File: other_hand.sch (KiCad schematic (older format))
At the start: 49 parts

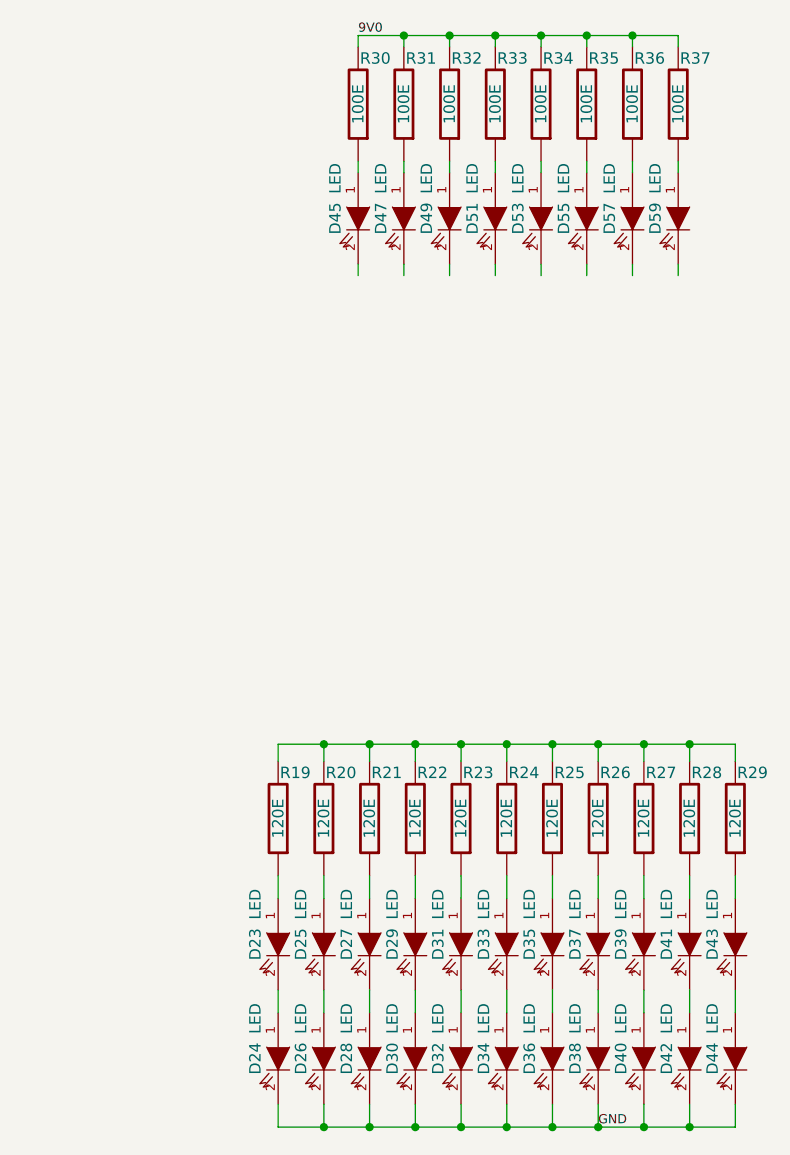
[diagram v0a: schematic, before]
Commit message: added the second Hand
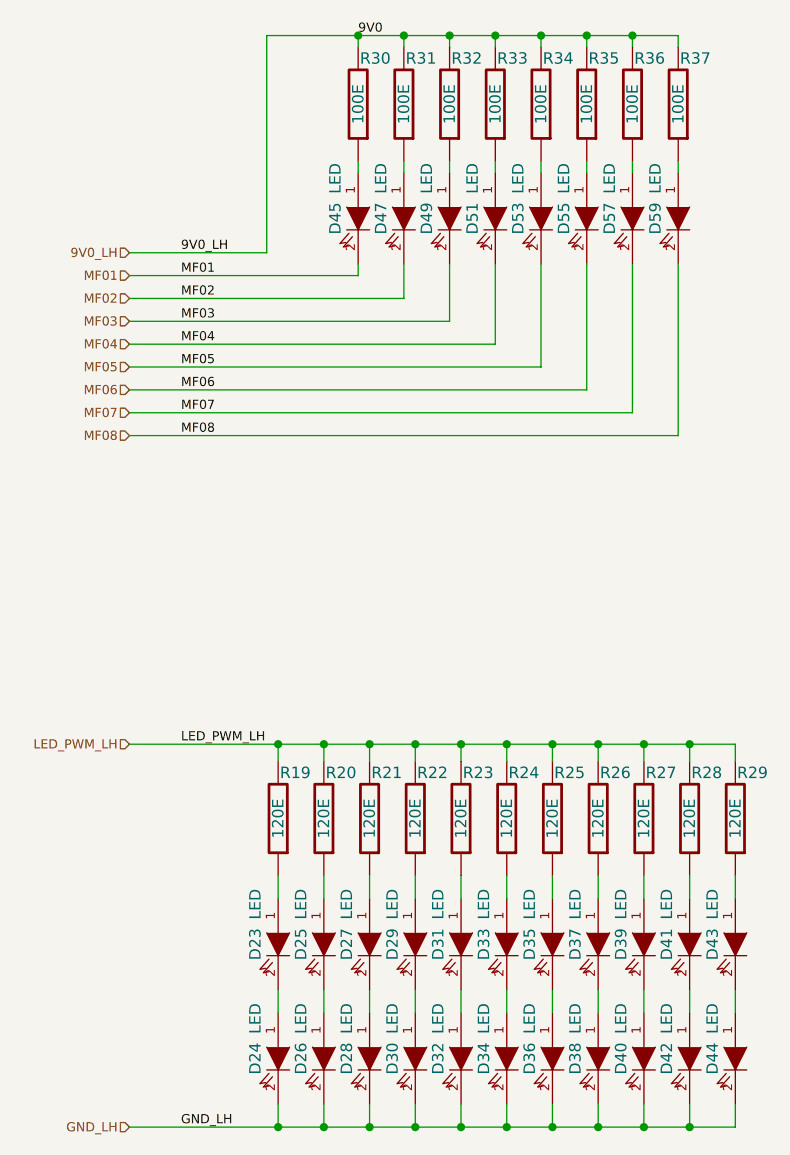
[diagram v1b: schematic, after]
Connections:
- net labels added: 9V0_LH, GND_LH, LED_PWM_LH, MF01, MF02, MF03, MF04, MF05, MF06, MF07, MF08
- net labels removed: GND
- wire segments 95 -> 81
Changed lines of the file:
@@
-EESchema Schematic File Version 2  date 7/4/2012 6:16:01 PM
+EESchema Schematic File Version 2  date 7/5/2012 5:41:43 PM
 LIBS:stfu
 LIBS:power
@@
 Sheet 2 2
 Title ""
-Date "4 jul 2012"
+Date "5 jul 2012"
 Rev ""
 Comp ""
@@
 Comment4 ""
 $EndDescr
+Text HLabel 6150 2600 0    40   Input ~ 0
+9V0_LH
+Text Label 6375 2600 0    40   ~ 0
+9V0_LH
+Connection ~ 7150 1650
+Wire Wire Line
+	6150 2600 6750 2600
+Wire Wire Line
+	6750 2600 6750 1650
+Wire Wire Line
+	6750 1650 8550 1650
+Connection ~ 6800 4750
+Wire Wire Line
+	6150 4750 8800 4750
+Wire Wire Line
+	8350 2650 8350 3300
+Wire Wire Line
+	8350 3300 6150 3300
+Wire Wire Line
+	7950 2650 7950 3100
+Wire Wire Line
+	7950 3100 6150 3100
+Wire Wire Line
+	7550 2650 7550 2900
+Wire Wire Line
+	7550 2900 6150 2900
+Wire Wire Line
+	6150 2700 7150 2700
+Connection ~ 8150 1650
+Wire Wire Line
+	8150 1650 8150 1700
+Connection ~ 7750 1650
+Wire Wire Line
+	7750 1650 7750 1700
+Connection ~ 7350 1650
+Wire Wire Line
+	7350 1650 7350 1700
+Wire Wire Line
+	7150 2700 7150 2650
+Wire Wire Line
+	8550 2250 8550 2200
+Wire Wire Line
+	8150 2250 8150 2200
+Wire Wire Line
+	7750 2250 7750 2200
+Wire Wire Line
+	7350 2250 7350 2200
+Wire Wire Line
+	7150 2200 7150 2250
+Wire Wire Line
+	7550 2200 7550 2250
+Wire Wire Line
+	7950 2200 7950 2250
+Wire Wire Line
+	8350 2200 8350 2250
+Wire Wire Line
+	7150 1650 7150 1700
+Wire Wire Line
+	8550 1650 8550 1700
+Wire Wire Line
+	7550 1650 7550 1700
+Connection ~ 7550 1650
+Wire Wire Line
+	7950 1650 7950 1700
+Connection ~ 7950 1650
+Wire Wire Line
+	8350 1700 8350 1650
+Connection ~ 8350 1650
+Connection ~ 7000 6425
+Connection ~ 8200 6425
+Connection ~ 8200 4750
+Connection ~ 8000 6425
+Connection ~ 7600 6425
+Connection ~ 7200 6425
+Wire Wire Line
+	8000 6425 8000 6325
+Wire Wire Line
+	7600 6425 7600 6325
+Wire Wire Line
+	7200 6425 7200 6325
+Wire Wire Line
+	8000 5825 8000 5925
+Wire Wire Line
+	7600 5825 7600 5925
+Wire Wire Line
+	7200 5825 7200 5925
+Wire Wire Line
+	8000 5325 8000 5425
+Wire Wire Line
+	7600 5325 7600 5425
+Wire Wire Line
+	7200 5325 7200 5425
+Connection ~ 7200 4750
+Wire Wire Line
+	7200 4750 7200 4825
+Connection ~ 7600 4750
+Wire Wire Line
+	7600 4750 7600 4825
+Connection ~ 8000 4750
+Wire Wire Line
+	8000 4750 8000 4825
+Wire Wire Line
+	8200 4750 8200 4825
+Wire Wire Line
+	7800 4750 7800 4825
+Connection ~ 7800 4750
+Wire Wire Line
+	7400 4750 7400 4825
+Connection ~ 7400 4750
+Wire Wire Line
+	7000 4750 7000 4825
+Wire Wire Line
+	7000 5325 7000 5425
+Wire Wire Line
+	7400 5325 7400 5425
+Wire Wire Line
+	7800 5325 7800 5425
+Wire Wire Line
+	8200 5325 8200 5425
+Wire Wire Line
+	7000 5825 7000 5925
+Wire Wire Line
+	7400 5825 7400 5925
+Wire Wire Line
+	7800 5825 7800 5925
+Wire Wire Line
+	8200 5825 8200 5925
+Wire Wire Line
+	8200 6425 8200 6325
+Wire Wire Line
+	7000 6425 7000 6325
+Wire Wire Line
+	7400 6425 7400 6325
+Connection ~ 7400 6425
+Wire Wire Line
+	7800 6425 7800 6325
+Connection ~ 7800 6425
+Connection ~ 8600 6425
+Wire Wire Line
+	8600 6325 8600 6425
+Wire Wire Line
+	8600 5825 8600 5925
+Wire Wire Line
+	8600 5325 8600 5425
+Connection ~ 8600 4750
+Wire Wire Line
+	8600 4825 8600 4750
+Wire Wire Line
+	8800 4750 8800 4825
+Wire Wire Line
+	8400 4750 8400 4825
+Connection ~ 8400 4750
+Wire Wire Line
+	8400 5325 8400 5425
+Wire Wire Line
+	8800 5325 8800 5425
+Wire Wire Line
+	8400 5825 8400 5925
+Wire Wire Line
+	8800 5825 8800 5925
+Wire Wire Line
+	8400 6425 8400 6325
+Wire Wire Line
+	8800 6325 8800 6425
+Connection ~ 8400 6425
+Wire Wire Line
+	6800 4750 6800 4825
+Wire Wire Line
+	6800 5325 6800 5425
+Wire Wire Line
+	6800 5825 6800 5925
+Wire Wire Line
+	6800 6425 6800 6325
+Connection ~ 7000 4750
+Wire Wire Line
+	6150 2800 7350 2800
+Wire Wire Line
+	7350 2800 7350 2650
+Wire Wire Line
+	6150 3000 7750 3000
+Wire Wire Line
+	7750 3000 7750 2650
+Wire Wire Line
+	6150 3200 8150 3200
+Wire Wire Line
+	8150 3200 8150 2650
+Wire Wire Line
+	6150 3400 8550 3400
+Wire Wire Line
+	8550 3400 8550 2650
+Wire Wire Line
+	8800 6425 6150 6425
+Connection ~ 6800 6425
+Text HLabel 6150 4750 0    40   Input ~ 0
+LED_PWM_LH
+Text HLabel 6150 6425 0    40   Input ~ 0
+GND_LH
+Text HLabel 6150 3400 0    40   Input ~ 0
+MF08
+Text HLabel 6150 3300 0    40   Input ~ 0
+MF07
+Text HLabel 6150 3200 0    40   Input ~ 0
+MF06
+Text HLabel 6150 3100 0    40   Input ~ 0
+MF05
+Text HLabel 6150 3000 0    40   Input ~ 0
+MF04
+Text HLabel 6150 2900 0    40   Input ~ 0
+MF03
+Text HLabel 6150 2800 0    40   Input ~ 0
+MF02
+Text HLabel 6150 2700 0    40   Input ~ 0
+MF01
+Text Label 6375 3400 0    40   ~ 0
+MF08
+Text Label 6375 3300 0    40   ~ 0
+MF07
+Text Label 6375 3200 0    40   ~ 0
+MF06
+Text Label 6375 3100 0    40   ~ 0
+MF05
+Text Label 6375 3000 0    40   ~ 0
+MF04
+Text Label 6375 2900 0    40   ~ 0
+MF03
+Text Label 6375 2800 0    40   ~ 0
+MF02
+Text Label 6375 2700 0    40   ~ 0
+MF01
+Text Label 6375 4750 0    40   ~ 0
+LED_PWM_LH
 $Comp
 L LED D23
@@
 	0    1    1    0
 $EndComp
-Text Label 8200 6425 0    40   ~ 0
-GND
+Text Label 6375 6425 0    40   ~ 0
+GND_LH
 $Comp
 L LED D31
@@
 	-1   0    0    1
 $EndComp
-Connection ~ 7000 4750
-Wire Wire Line
-	8800 4750 8600 4750
-Wire Wire Line
-	8600 4750 8400 4750
-Wire Wire Line
-	8400 4750 8200 4750
-Wire Wire Line
-	8200 4750 8000 4750
-Wire Wire Line
-	8000 4750 7800 4750
-Wire Wire Line
-	7800 4750 7600 4750
-Wire Wire Line
-	7600 4750 7400 4750
-Wire Wire Line
-	7400 4750 7200 4750
-Wire Wire Line
-	7200 4750 7000 4750
-Wire Wire Line
-	7000 4750 6800 4750
-Wire Wire Line
-	6800 6425 6800 6325
-Wire Wire Line
-	6800 5825 6800 5925
-Wire Wire Line
-	6800 5325 6800 5425
-Wire Wire Line
-	6800 4750 6800 4825
-Connection ~ 8400 6425
-Wire Wire Line
-	8800 6425 8800 6325
-Wire Wire Line
-	8400 6425 8400 6325
-Wire Wire Line
-	8800 5825 8800 5925
-Wire Wire Line
-	8400 5825 8400 5925
-Wire Wire Line
-	8800 5325 8800 5425
-Wire Wire Line
-	8400 5325 8400 5425
-Connection ~ 8400 4750
-Wire Wire Line
-	8400 4750 8400 4825
-Wire Wire Line
-	8800 4825 8800 4750
-Wire Wire Line
-	8600 4825 8600 4750
-Connection ~ 8600 4750
-Wire Wire Line
-	8600 5325 8600 5425
-Wire Wire Line
-	8600 5825 8600 5925
-Wire Wire Line
-	8600 6325 8600 6425
-Connection ~ 8600 6425
-Connection ~ 7800 6425
-Wire Wire Line
-	7800 6425 7800 6325
-Connection ~ 7400 6425
-Wire Wire Line
-	7400 6425 7400 6325
-Wire Wire Line
-	7000 6425 7000 6325
-Wire Wire Line
-	8200 6425 8200 6325
-Wire Wire Line
-	8200 5825 8200 5925
-Wire Wire Line
-	7800 5825 7800 5925
-Wire Wire Line
-	7400 5825 7400 5925
-Wire Wire Line
-	7000 5825 7000 5925
-Wire Wire Line
-	8200 5325 8200 5425
-Wire Wire Line
-	7800 5325 7800 5425
-Wire Wire Line
-	7400 5325 7400 5425
-Wire Wire Line
-	7000 5325 7000 5425
-Wire Wire Line
-	7000 4750 7000 4825
-Connection ~ 7400 4750
-Wire Wire Line
-	7400 4750 7400 4825
-Connection ~ 7800 4750
-Wire Wire Line
-	7800 4750 7800 4825
-Wire Wire Line
-	8200 4750 8200 4825
-Wire Wire Line
-	8000 4750 8000 4825
-Connection ~ 8000 4750
-Wire Wire Line
-	7600 4750 7600 4825
-Connection ~ 7600 4750
-Wire Wire Line
-	7200 4750 7200 4825
-Connection ~ 7200 4750
-Wire Wire Line
-	7200 5325 7200 5425
-Wire Wire Line
-	7600 5325 7600 5425
-Wire Wire Line
-	8000 5325 8000 5425
-Wire Wire Line
-	7200 5825 7200 5925
-Wire Wire Line
-	7600 5825 7600 5925
-Wire Wire Line
-	8000 5825 8000 5925
-Wire Wire Line
-	7200 6425 7200 6325
-Wire Wire Line
-	7600 6425 7600 6325
-Wire Wire Line
-	8000 6425 8000 6325
-Connection ~ 7200 6425
-Connection ~ 7600 6425
-Connection ~ 8000 6425
-Connection ~ 8200 4750
-Connection ~ 8200 6425
-Wire Wire Line
-	8800 6425 8600 6425
-Wire Wire Line
-	8600 6425 8400 6425
-Wire Wire Line
-	8400 6425 8200 6425
-Wire Wire Line
-	8200 6425 8000 6425
-Wire Wire Line
-	8000 6425 7800 6425
-Wire Wire Line
-	7800 6425 7600 6425
-Wire Wire Line
-	7600 6425 7400 6425
-Wire Wire Line
-	7400 6425 7200 6425
-Wire Wire Line
-	7200 6425 7000 6425
-Wire Wire Line
-	7000 6425 6800 6425
-Connection ~ 7000 6425
 $Comp
 L LED D45
@@
 Text Label 7150 1650 0    40   ~ 0
 9V0
-Connection ~ 8350 1650
-Wire Wire Line
-	8350 1700 8350 1650
-Connection ~ 7950 1650
-Wire Wire Line
-	7950 1650 7950 1700
-Connection ~ 7550 1650
-Wire Wire Line
-	7550 1650 7550 1700
-Wire Wire Line
-	8550 1650 8550 1700
-Wire Wire Line
-	7150 1650 7350 1650
-Wire Wire Line
-	7350 1650 7550 1650
-Wire Wire Line
-	7550 1650 7750 1650
-Wire Wire Line
-	7750 1650 7950 1650
-Wire Wire Line
-	7950 1650 8150 1650
-Wire Wire Line
-	8150 1650 8350 1650
-Wire Wire Line
-	8350 1650 8550 1650
-Wire Wire Line
-	7150 1700 7150 1650
-Wire Wire Line
-	8550 2650 8550 2700
-Wire Wire Line
-	8150 2650 8150 2700
-Wire Wire Line
-	7750 2650 7750 2700
-Wire Wire Line
-	7350 2650 7350 2700
-Wire Wire Line
-	8350 2200 8350 2250
-Wire Wire Line
-	7950 2200 7950 2250
-Wire Wire Line
-	7550 2200 7550 2250
-Wire Wire Line
-	7150 2200 7150 2250
-Wire Wire Line
-	7350 2250 7350 2200
-Wire Wire Line
-	7750 2250 7750 2200
-Wire Wire Line
-	8150 2250 8150 2200
-Wire Wire Line
-	8550 2250 8550 2200
-Wire Wire Line
-	7150 2650 7150 2700
-Wire Wire Line
-	7550 2650 7550 2700
-Wire Wire Line
-	7950 2650 7950 2700
-Wire Wire Line
-	8350 2650 8350 2700
-Wire Wire Line
-	7350 1700 7350 1650
-Connection ~ 7350 1650
-Wire Wire Line
-	7750 1650 7750 1700
-Connection ~ 7750 1650
-Wire Wire Line
-	8150 1650 8150 1700
-Connection ~ 8150 1650
 $EndSCHEMATC
